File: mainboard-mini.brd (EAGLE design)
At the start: 56.8 x 67.3 mm, 104 parts, among them IC1 XC6206P332MR, IC2 LM2901, IC3 NC7SZ10P6X, IC4 STM32F103RBT6, IC5 TDA2822D, IC6 SN65HVD230, IC7 RT8259GE, Q1 8MHz

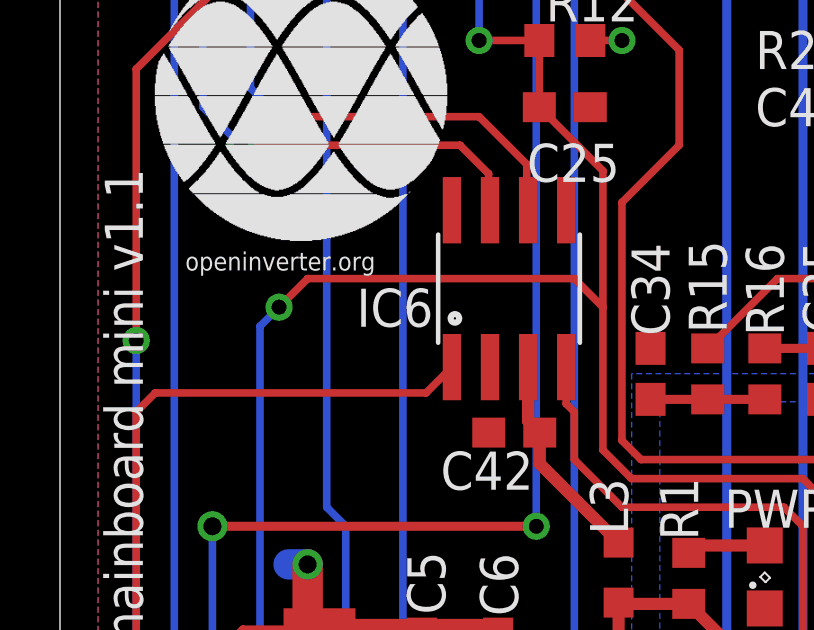
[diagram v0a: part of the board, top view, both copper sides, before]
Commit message: Added 10k resistor to CAN transceiver RS pin
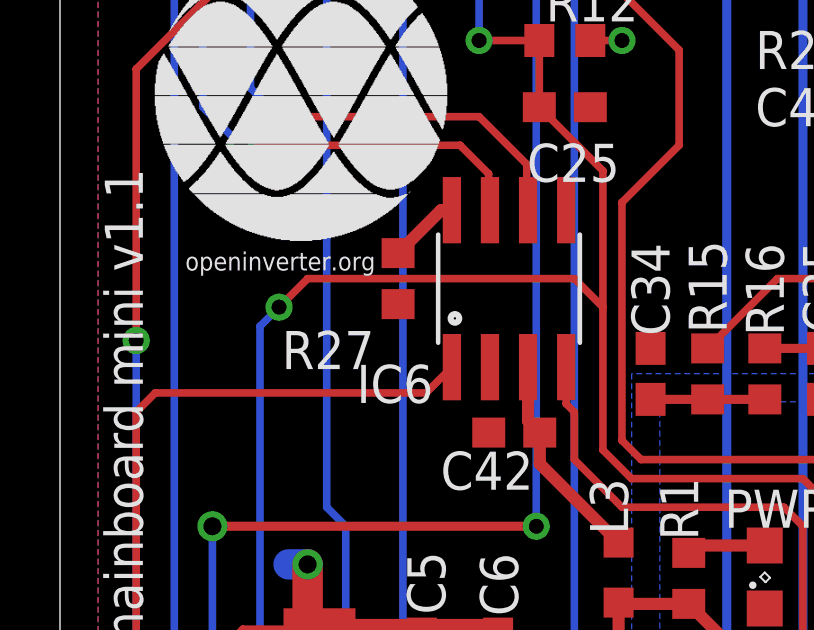
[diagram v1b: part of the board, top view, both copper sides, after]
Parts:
- added R27: 10k, rcl:R0603
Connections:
- new net N$24: IC6.8, R27.2
- net GND: now also R27.1
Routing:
- net N$24: track 0.00 -> 2.38 mm
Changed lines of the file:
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@@
 <element name="IC6" library="SparkFun-DigitalIC" package="SO08" value="SN65HVD230" x="14.9675" y="49.195" smashed="yes">
 <attribute name="VALUE" x="13.6975" y="48.56" size="0.4064" layer="27"/>
-<attribute name="NAME" x="9.8875" y="47.925" size="1.27" layer="25"/>
+<attribute name="NAME" x="9.8875" y="45.385" size="1.27" layer="25"/>
 </element>
 <element name="C32" library="rcl" package="C0603" value="1nF" x="34.29" y="38.735" rot="R90"/>
@@
 <element name="C2" library="rcl" package="C0603" value="10µ" x="12.3825" y="22.86"/>
 <element name="SJ3" library="SparkFun-Passives" package="SJ_3_PASTE2&amp;3" value="" x="13.6525" y="18.57375" rot="R180"/>
+<element name="R27" library="rcl" package="R0603" value="10k" x="11.27125" y="49.53" smashed="yes" rot="R90">
+<attribute name="NAME" x="10.4775" y="47.78375" size="1.27" layer="25" rot="R180"/>
+<attribute name="VALUE" x="13.17625" y="48.895" size="1.27" layer="27" rot="R90"/>
+</element>
 </elements>
 <signals>
@@
 <wire x1="45.3" y1="16.295" x2="45.085" y2="16.295" width="0.254" layer="1"/>
 <contactref element="C2" pad="2"/>
+<contactref element="R27" pad="1"/>
 </signal>
 <signal name="VCC">
@@
 <wire x1="11.9625" y1="18.57375" x2="11.01" y2="17.62125" width="0.254" layer="1"/>
 </signal>
+<signal name="N$24">
+<contactref element="IC6" pad="8"/>
+<contactref element="R27" pad="2"/>
+<wire x1="11.27125" y1="50.38" x2="12.70245" y2="51.8112" width="0.4064" layer="1"/>
+<wire x1="12.70245" y1="51.8112" x2="13.0625" y2="51.8112" width="0.4064" layer="1"/>
+</signal>
 </signals>
